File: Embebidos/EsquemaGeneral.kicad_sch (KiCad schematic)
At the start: 0 parts

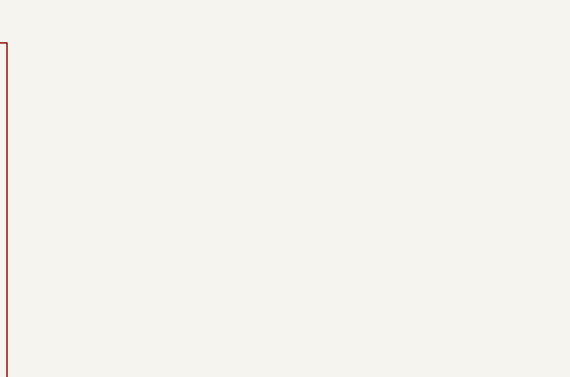
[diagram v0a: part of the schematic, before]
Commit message: LDR module adittion
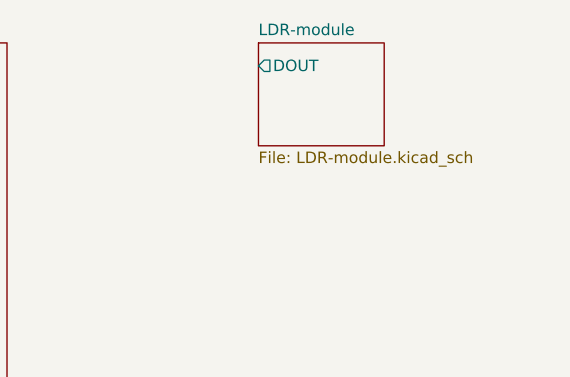
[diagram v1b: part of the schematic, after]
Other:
- added sheet LDR-module (LDR-module.kicad_sch)
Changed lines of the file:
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@@
+    )
+  )
+  (sheet (at 154.94 38.1) (size 13.97 11.43) (fields_autoplaced)
+    (stroke (width 0.1524) (type solid) (color 0 0 0 0))
+    (fill (color 0 0 0 0.0000))
+    (property "Sheet name" "LDR-module" (id 0) (at 154.94 37.3884 0)
+      (effects (font (size 1.27 1.27)) (justify left bottom))
+    )
+    (property "Sheet file" "LDR-module.kicad_sch" (id 1) (at 154.94 50.1146 0)
+      (effects (font (size 1.27 1.27)) (justify left top))
+    )
+    (pin "DOUT" output (at 154.94 40.64 180)
+      (effects (font (size 1.27 1.27)) (justify left))
     )
   )
@@
     (path "/e1535036-5d36-405f-bb86-3819621c4f23" (page "2"))
     (path "/cc31ce4a-ad9b-4479-bbdf-beeab98489e8" (page "3"))
+    (path "/d06b1486-3743-4568-bb86-22a0f801ae16" (page "4"))
   )
   (symbol_instances
@@
       (reference "#PWR?") (unit 1) (value "~") (footprint "")
     )
+    (path "/d06b1486-3743-4568-bb86-22a0f801ae16/4013d787-82a8-4caa-b357-a11ef5ca8bab"
+      (reference "#PWR?") (unit 1) (value "GND") (footprint "")
+    )
+    (path "/d06b1486-3743-4568-bb86-22a0f801ae16/5217286f-63fa-4738-8dbe-0c3a62478e5c"
+      (reference "#PWR?") (unit 1) (value "GND") (footprint "")
+    )
     (path "/e1535036-5d36-405f-bb86-3819621c4f23/5589c2d1-2314-45c5-8084-3b63ebe19fa8"
       (reference "#PWR?") (unit 1) (value "GND") (footprint "")
@@
     (path "/e1535036-5d36-405f-bb86-3819621c4f23/b33365c2-a488-4a72-841c-399554d1dfe3"
       (reference "#PWR?") (unit 1) (value "+3.3V") (footprint "")
+    )
+    (path "/d06b1486-3743-4568-bb86-22a0f801ae16/b99111ad-6e28-472f-a7c1-e59a2424250c"
+      (reference "#PWR?") (unit 1) (value "+5V") (footprint "")
+    )
+    (path "/d06b1486-3743-4568-bb86-22a0f801ae16/baccec78-2091-407b-9f3d-6da8242e6b6b"
+      (reference "#PWR?") (unit 1) (value "GND") (footprint "")
+    )
+    (path "/d06b1486-3743-4568-bb86-22a0f801ae16/c9d628d3-72db-42f7-81c2-74a7c7ce8b2e"
+      (reference "#PWR?") (unit 1) (value "+5V") (footprint "")
     )
     (path "/e1535036-5d36-405f-bb86-3819621c4f23/d8200fb9-692f-4a11-83a1-7fda17199f17"
@@
       (reference "C4") (unit 1) (value "0.1u") (footprint "")
     )
+    (path "/d06b1486-3743-4568-bb86-22a0f801ae16/eb96f5b1-755c-4d95-a6fd-44e7416fb461"
+      (reference "C?") (unit 1) (value "104") (footprint "")
+    )
+    (path "/d06b1486-3743-4568-bb86-22a0f801ae16/ec241fc1-c884-4631-85b0-6ac2882abcec"
+      (reference "C?") (unit 1) (value "104") (footprint "")
+    )
     (path "/e1535036-5d36-405f-bb86-3819621c4f23/ba412eb5-13bb-4cbc-b2d7-7f2ddb11dbbd"
       (reference "D1") (unit 1) (value "LED_ON") (footprint "")
@@
       (reference "D2") (unit 1) (value "LED_HW") (footprint "")
     )
+    (path "/d06b1486-3743-4568-bb86-22a0f801ae16/9ce37f5d-4ced-4e2d-a6bd-e720d1623000"
+      (reference "D?") (unit 1) (value "Detection LED") (footprint "")
+    )
+    (path "/d06b1486-3743-4568-bb86-22a0f801ae16/eff1643e-1700-4d04-9e5b-906bea3f1134"
+      (reference "D?") (unit 1) (value "Power LED") (footprint "")
+    )
     (path "/e1535036-5d36-405f-bb86-3819621c4f23/d7ff11f1-9ba3-48a8-b392-f827773e8cf2"
       (reference "IC1") (unit 1) (value "ESP32-WROVER-B__8MB_") (footprint "ESP32WROVERB8MB")
@@
       (reference "R13") (unit 1) (value "~") (footprint "")
     )
+    (path "/d06b1486-3743-4568-bb86-22a0f801ae16/22d8495c-c8d6-4d86-8447-7c0d31417765"
+      (reference "R?") (unit 1) (value "1K") (footprint "")
+    )
+    (path "/d06b1486-3743-4568-bb86-22a0f801ae16/7ab9cb54-b83f-4986-88b1-5139b9e39300"
+      (reference "R?") (unit 1) (value "1K") (footprint "")
+    )
+    (path "/d06b1486-3743-4568-bb86-22a0f801ae16/9c6fcf17-3cde-4100-85b2-e301753b471d"
+      (reference "R?") (unit 1) (value "LDR07") (footprint "OptoDevice:R_LDR_5.1x4.3mm_P3.4mm_Vertical")
+    )
+    (path "/d06b1486-3743-4568-bb86-22a0f801ae16/b27e07ef-9631-4d9f-912c-6292d57b8593"
+      (reference "R?") (unit 1) (value "10K") (footprint "")
+    )
+    (path "/d06b1486-3743-4568-bb86-22a0f801ae16/88d00d85-45cc-430a-a61f-4b7ae6be4610"
+      (reference "RV?") (unit 1) (value "10K") (footprint "")
+    )
     (path "/e1535036-5d36-405f-bb86-3819621c4f23/98b4f046-6768-4ae2-81aa-dbcfff0dac71"
       (reference "SW1") (unit 1) (value "SW_Boot") (footprint "")
@@
       (reference "U1") (unit 1) (value "~") (footprint "")
     )
-  )
+    (path "/d06b1486-3743-4568-bb86-22a0f801ae16/4186dce2-6fa5-4e12-a42f-3f810169d21c"
+      (reference "U?") (unit 1) (value "LM358") (footprint "")
+    )
+    (path "/d06b1486-3743-4568-bb86-22a0f801ae16/71f03a5b-85ab-4dca-8c4e-871d91590e0f"
+      (reference "U?") (unit 2) (value "LM358") (footprint "")
+    )
+    (path "/d06b1486-3743-4568-bb86-22a0f801ae16/880375a2-ae6e-4fc5-b9c3-185e23ee3394"
+      (reference "U?") (unit 3) (value "LM358") (footprint "")
+    )
+  )

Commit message: Alimentacion
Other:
- added sheet Alimentacion (alimentacion.kicad_sch)
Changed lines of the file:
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@@
+    )
+  )
+  (sheet (at 143.51 68.58) (size 25.4 17.78) (fields_autoplaced)
+    (stroke (width 0.1524) (type solid) (color 0 0 0 0))
+    (fill (color 0 0 0 0.0000))
+    (property "Sheet name" "Alimentacion" (id 0) (at 143.51 67.8684 0)
+      (effects (font (size 1.27 1.27)) (justify left bottom))
+    )
+    (property "Sheet file" "alimentacion.kicad_sch" (id 1) (at 143.51 86.9446 0)
+      (effects (font (size 1.27 1.27)) (justify left top))
     )
   )
@@
     (path "/cc31ce4a-ad9b-4479-bbdf-beeab98489e8" (page "3"))
     (path "/d06b1486-3743-4568-bb86-22a0f801ae16" (page "4"))
+    (path "/dbd907f8-459e-4808-a4de-1506df10bcec" (page "5"))
   )
   (symbol_instances
+    (path "/dbd907f8-459e-4808-a4de-1506df10bcec/ed6d1bb6-c7b9-4396-bbf4-ac0ba0ed69e7"
+      (reference "#PWR01") (unit 1) (value "+5V") (footprint "")
+    )
+    (path "/dbd907f8-459e-4808-a4de-1506df10bcec/0041a742-b80a-422d-8252-cf0a19f2b7cc"
+      (reference "#PWR02") (unit 1) (value "GND") (footprint "")
+    )
+    (path "/dbd907f8-459e-4808-a4de-1506df10bcec/9c97d272-adf6-449e-be00-9f638fb332c3"
+      (reference "#PWR03") (unit 1) (value "GND") (footprint "")
+    )
+    (path "/dbd907f8-459e-4808-a4de-1506df10bcec/1c1f5fba-a486-4535-ba12-32ef71bea7fe"
+      (reference "#PWR04") (unit 1) (value "GND") (footprint "")
+    )
+    (path "/dbd907f8-459e-4808-a4de-1506df10bcec/0e164718-2b92-41b7-90c8-76f6256b7293"
+      (reference "#PWR05") (unit 1) (value "GND") (footprint "")
+    )
+    (path "/dbd907f8-459e-4808-a4de-1506df10bcec/80408b97-0903-4a9d-8956-e7f0b1581480"
+      (reference "#PWR07") (unit 1) (value "GND") (footprint "")
+    )
+    (path "/dbd907f8-459e-4808-a4de-1506df10bcec/16558b76-52bf-432b-83d5-ef5d4fcf5979"
+      (reference "#PWR08") (unit 1) (value "GND") (footprint "")
+    )
+    (path "/dbd907f8-459e-4808-a4de-1506df10bcec/5f400297-26fd-4587-9ebe-aca6530094f5"
+      (reference "#PWR010") (unit 1) (value "GND") (footprint "")
+    )
     (path "/cc31ce4a-ad9b-4479-bbdf-beeab98489e8/1ed76e64-2b46-4121-8e2c-15569733294f"
       (reference "#PWR?") (unit 1) (value "~") (footprint "")
@@
       (reference "#PWR?") (unit 1) (value "GND") (footprint "")
     )
+    (path "/dbd907f8-459e-4808-a4de-1506df10bcec/d13e6b54-b8c7-4c32-bd8f-a5ab92c37b48"
+      (reference "C1") (unit 1) (value "100u") (footprint "")
+    )
     (path "/e1535036-5d36-405f-bb86-3819621c4f23/d81047d0-6c1b-4589-b37f-eb5534216b82"
       (reference "C1") (unit 1) (value "22uF") (footprint "")
@@
       (reference "C2") (unit 1) (value "0.1uF") (footprint "")
     )
+    (path "/dbd907f8-459e-4808-a4de-1506df10bcec/6e0dc09e-edeb-4109-9ddb-db3b0f6e2232"
+      (reference "C2") (unit 1) (value "1u") (footprint "Capacitor_SMD:C_0603_1608Metric_Pad1.08x0.95mm_HandSolder")
+    )
     (path "/cc31ce4a-ad9b-4479-bbdf-beeab98489e8/d3842c7f-088a-42ca-8559-a68caf720c9c"
       (reference "C2") (unit 1) (value "~") (footprint "")
@@
       (reference "C3") (unit 1) (value "~") (footprint "")
     )
+    (path "/dbd907f8-459e-4808-a4de-1506df10bcec/a03c2b30-48fe-4d16-a726-60177bf460a2"
+      (reference "C3") (unit 1) (value "330u") (footprint "")
+    )
+    (path "/dbd907f8-459e-4808-a4de-1506df10bcec/55e8fdb6-200e-4de9-ba1b-3a737aaa80ec"
+      (reference "C4") (unit 1) (value "100n") (footprint "")
+    )
     (path "/e1535036-5d36-405f-bb86-3819621c4f23/88b4c3b5-cdba-451d-bfa9-6540b576b863"
       (reference "C4") (unit 1) (value "0.1u") (footprint "")
     )
+    (path "/dbd907f8-459e-4808-a4de-1506df10bcec/c1211a09-1b08-468f-8928-5e411f9c2caa"
+      (reference "C5") (unit 1) (value "10u") (footprint "")
+    )
+    (path "/dbd907f8-459e-4808-a4de-1506df10bcec/e54509d2-25c2-432b-896c-deb582dce5b9"
+      (reference "C6") (unit 1) (value "1u") (footprint "")
+    )
+    (path "/dbd907f8-459e-4808-a4de-1506df10bcec/0d1f3cdb-ddc7-432c-81b7-220d04c08ea6"
+      (reference "C7") (unit 1) (value "10u") (footprint "")
+    )
+    (path "/dbd907f8-459e-4808-a4de-1506df10bcec/e4d3e0a4-6f39-4d37-bd7d-1d39c8cd7a3a"
+      (reference "C10") (unit 1) (value "10u") (footprint "")
+    )
+    (path "/dbd907f8-459e-4808-a4de-1506df10bcec/66650572-4c7e-4c10-b9e5-653731ee077b"
+      (reference "C11") (unit 1) (value "0.1u") (footprint "")
+    )
     (path "/d06b1486-3743-4568-bb86-22a0f801ae16/eb96f5b1-755c-4d95-a6fd-44e7416fb461"
       (reference "C?") (unit 1) (value "104") (footprint "")
@@
       (reference "IC1") (unit 1) (value "ESP32-WROVER-B__8MB_") (footprint "ESP32WROVERB8MB")
     )
+    (path "/dbd907f8-459e-4808-a4de-1506df10bcec/0e1ff7fd-ba1b-40b3-9a6e-c766f0ee9f37"
+      (reference "J1") (unit 1) (value "Conn_01x02_Male") (footprint "")
+    )
     (path "/cc31ce4a-ad9b-4479-bbdf-beeab98489e8/11991380-bb17-440d-afe9-cc63c353105e"
       (reference "J1") (unit 1) (value "~") (footprint "")
     )
+    (path "/dbd907f8-459e-4808-a4de-1506df10bcec/d8609417-ed01-4857-9622-08c7dd58c715"
+      (reference "J2") (unit 1) (value "Conn_01x02_Male") (footprint "")
+    )
+    (path "/dbd907f8-459e-4808-a4de-1506df10bcec/3888a4ed-7588-402a-ae65-74960c0ee3bd"
+      (reference "J4") (unit 1) (value "Conn_01x02_Male") (footprint "")
+    )
     (path "/cc31ce4a-ad9b-4479-bbdf-beeab98489e8/a42fec27-ea7c-440f-bb39-75dc4a60a465"
       (reference "Q1") (unit 1) (value "~") (footprint "")
@@
       (reference "R1") (unit 1) (value "~") (footprint "")
     )
+    (path "/dbd907f8-459e-4808-a4de-1506df10bcec/73cbc269-00cf-4f9a-bc04-87d31a3daff5"
+      (reference "R1") (unit 1) (value "100k") (footprint "")
+    )
     (path "/e1535036-5d36-405f-bb86-3819621c4f23/55552316-eba6-4d9e-a3f8-1729b8722f94"
       (reference "R2") (unit 1) (value "~") (footprint "")
     )
+    (path "/dbd907f8-459e-4808-a4de-1506df10bcec/9f59bb4f-be3c-48d9-88d7-030aeb1df0a8"
+      (reference "R2") (unit 1) (value "43k") (footprint "")
+    )
     (path "/cc31ce4a-ad9b-4479-bbdf-beeab98489e8/d811644f-126a-4254-85ba-a5ad3fc5423e"
       (reference "R2") (unit 1) (value "~") (footprint "")
@@
       (reference "R3") (unit 1) (value "~") (footprint "")
     )
+    (path "/dbd907f8-459e-4808-a4de-1506df10bcec/7526a878-a4c6-44a0-9ee2-ff93a1dcbd8e"
+      (reference "R3") (unit 1) (value "470") (footprint "")
+    )
+    (path "/dbd907f8-459e-4808-a4de-1506df10bcec/7d516aa0-42ed-4639-8990-e3ca2173c56f"
+      (reference "R4") (unit 1) (value "R") (footprint "")
+    )
     (path "/e1535036-5d36-405f-bb86-3819621c4f23/b2627254-0e80-4ec2-a767-9041b9b7f6ac"
       (reference "R4") (unit 1) (value "4.7k") (footprint "")
     )
+    (path "/dbd907f8-459e-4808-a4de-1506df10bcec/9bf31652-caac-43bb-af95-4b40b93971a9"
+      (reference "R5") (unit 1) (value "R") (footprint "")
+    )
     (path "/e1535036-5d36-405f-bb86-3819621c4f23/de055332-b1eb-4790-bdc4-825a8b3d86ae"
       (reference "R5") (unit 1) (value "4.7k") (footprint "")
@@
       (reference "SW2") (unit 1) (value "SW_Reset") (footprint "")
     )
+    (path "/dbd907f8-459e-4808-a4de-1506df10bcec/15d46b7e-438e-4017-936e-9a2fba6b1382"
+      (reference "U1") (unit 1) (value "MIC29302WT") (footprint "Package_TO_SOT_THT:TO-220-5_P3.4x3.7mm_StaggerEven_Lead3.8mm_Vertical")
+    )
     (path "/cc31ce4a-ad9b-4479-bbdf-beeab98489e8/8f700339-c9dd-4565-bc82-3d26ce7b2743"
       (reference "U1") (unit 1) (value "~") (footprint "")
     )
+    (path "/dbd907f8-459e-4808-a4de-1506df10bcec/a332eee4-8e5c-479e-9847-1890b457546d"
+      (reference "U2") (unit 1) (value "SPX3819M5-L-3-3") (footprint "Package_TO_SOT_SMD:SOT-23-5")
+    )
+    (path "/dbd907f8-459e-4808-a4de-1506df10bcec/c52adfc4-f7f4-42f8-923e-2dbea160665b"
+      (reference "U4") (unit 1) (value "MIC5219-3.3YM5") (footprint "Package_TO_SOT_SMD:SOT-23-5")
+    )
     (path "/d06b1486-3743-4568-bb86-22a0f801ae16/4186dce2-6fa5-4e12-a42f-3f810169d21c"

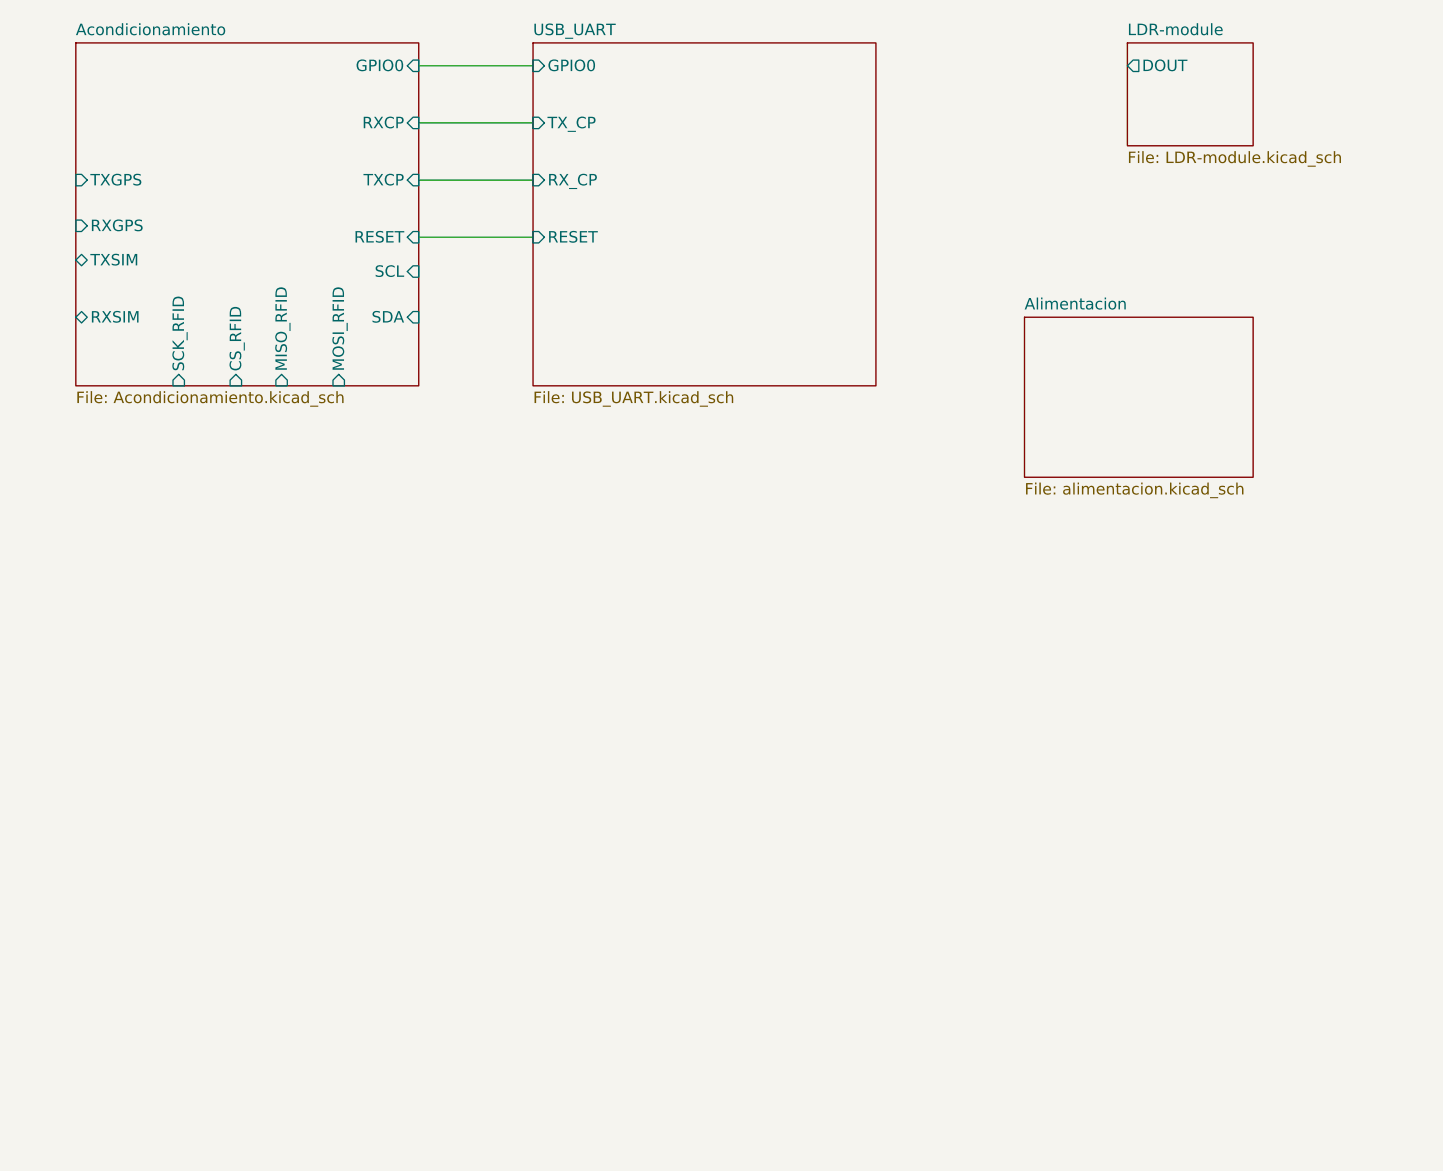
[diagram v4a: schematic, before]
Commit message: Luces delanteras, traseras, pantalla, e infrarrojo
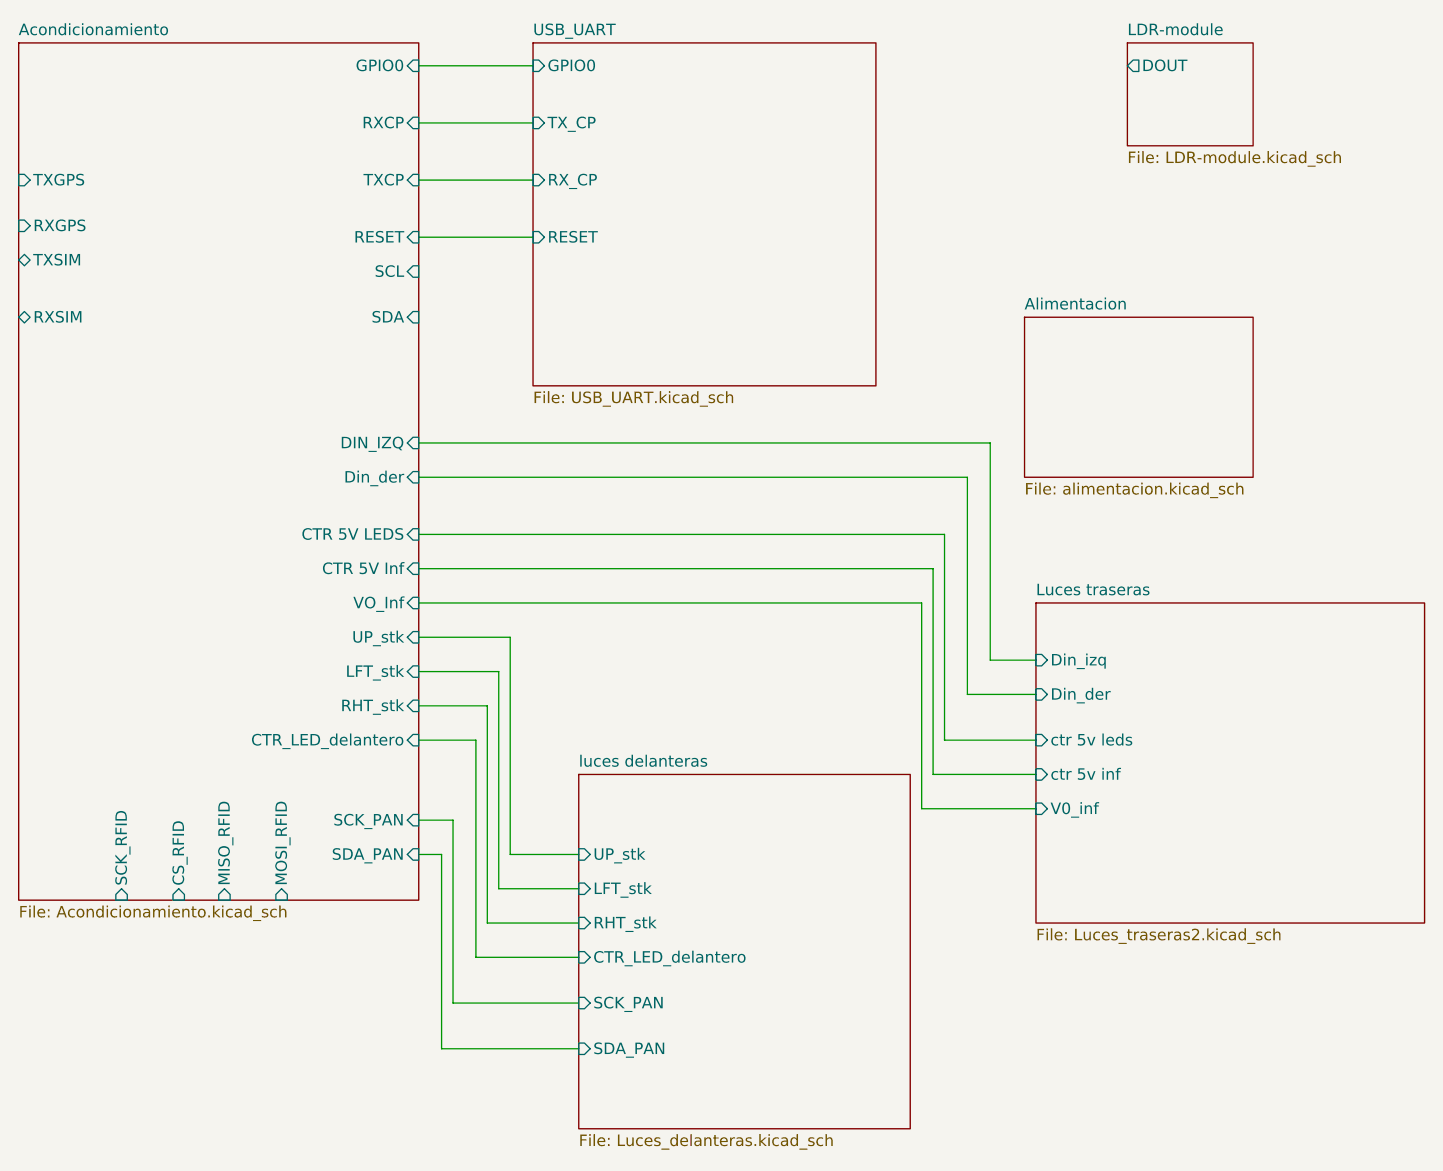
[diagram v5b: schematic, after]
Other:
- added sheet Luces traseras (Luces_traseras2.kicad_sch)
- added sheet luces delanteras (Luces_delanteras.kicad_sch)
- sheet Acondicionamiento ports: added CTR 5V Inf, CTR 5V LEDS, CTR_LED_delantero, DIN_IZQ, Din_der, LFT_stk, RHT_stk, SCK_PAN, SDA_PAN, UP_stk, VO_Inf; removed none
